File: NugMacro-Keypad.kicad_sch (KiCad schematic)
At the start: 16 parts

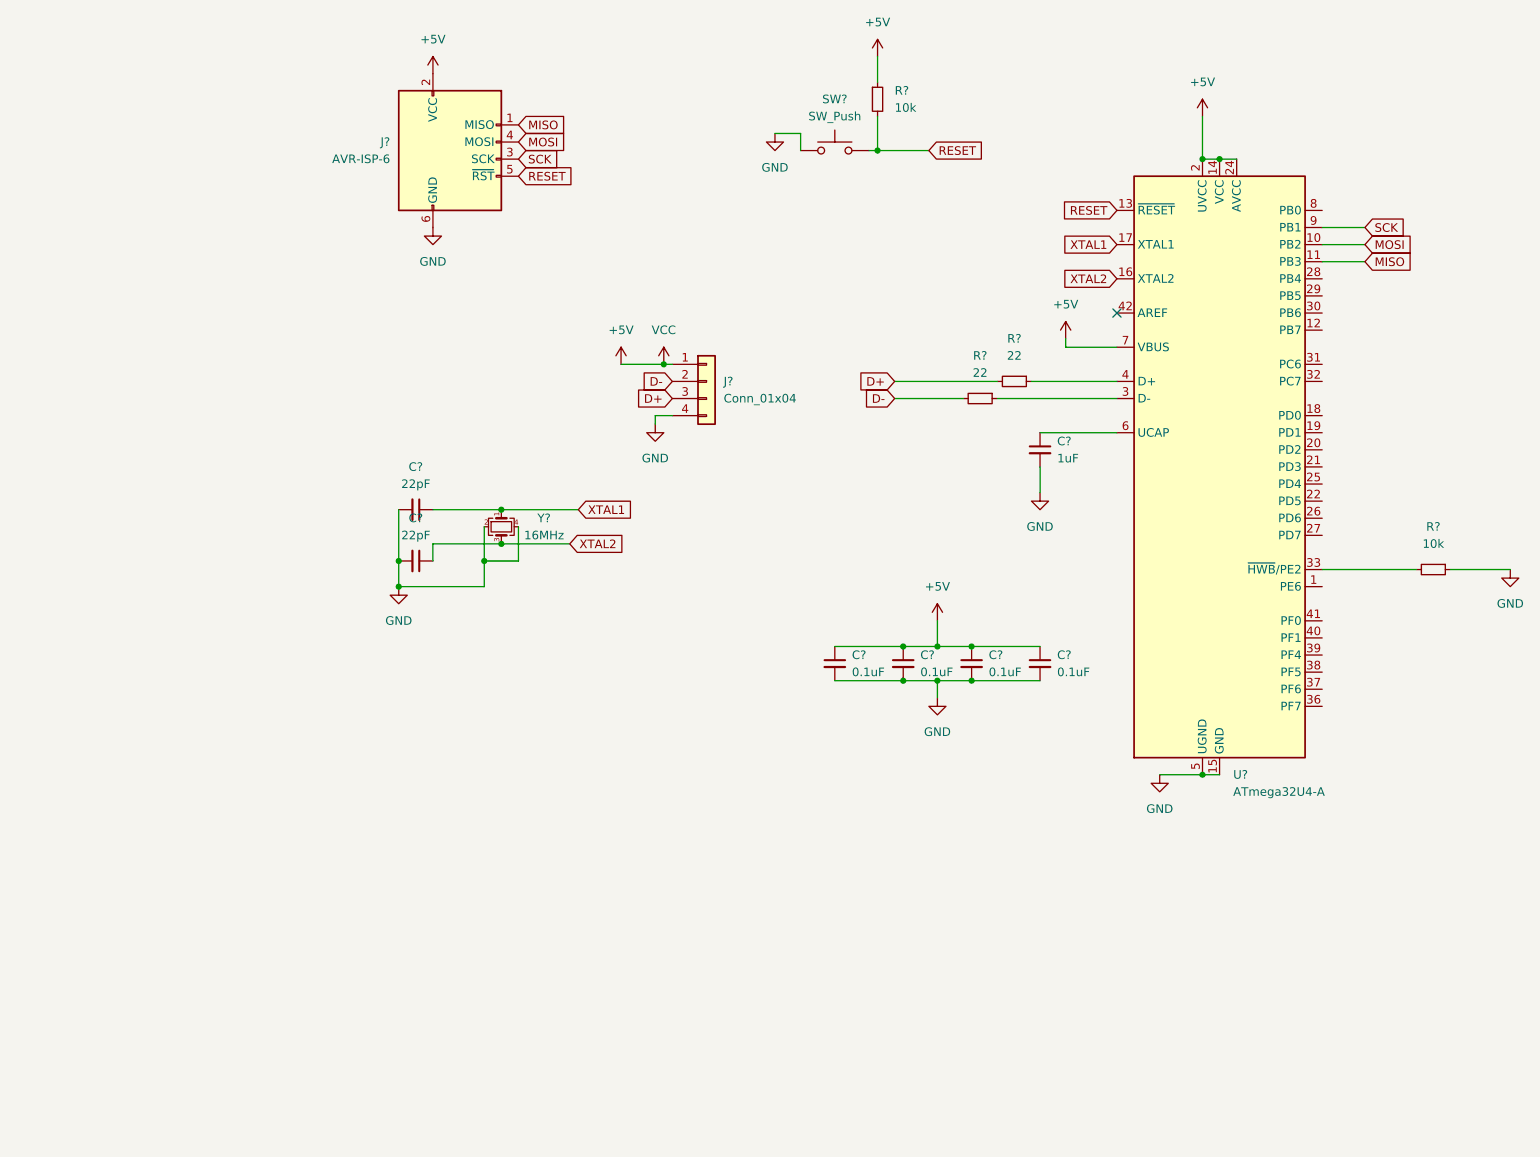
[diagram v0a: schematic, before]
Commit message: schema finished with footprints assigned
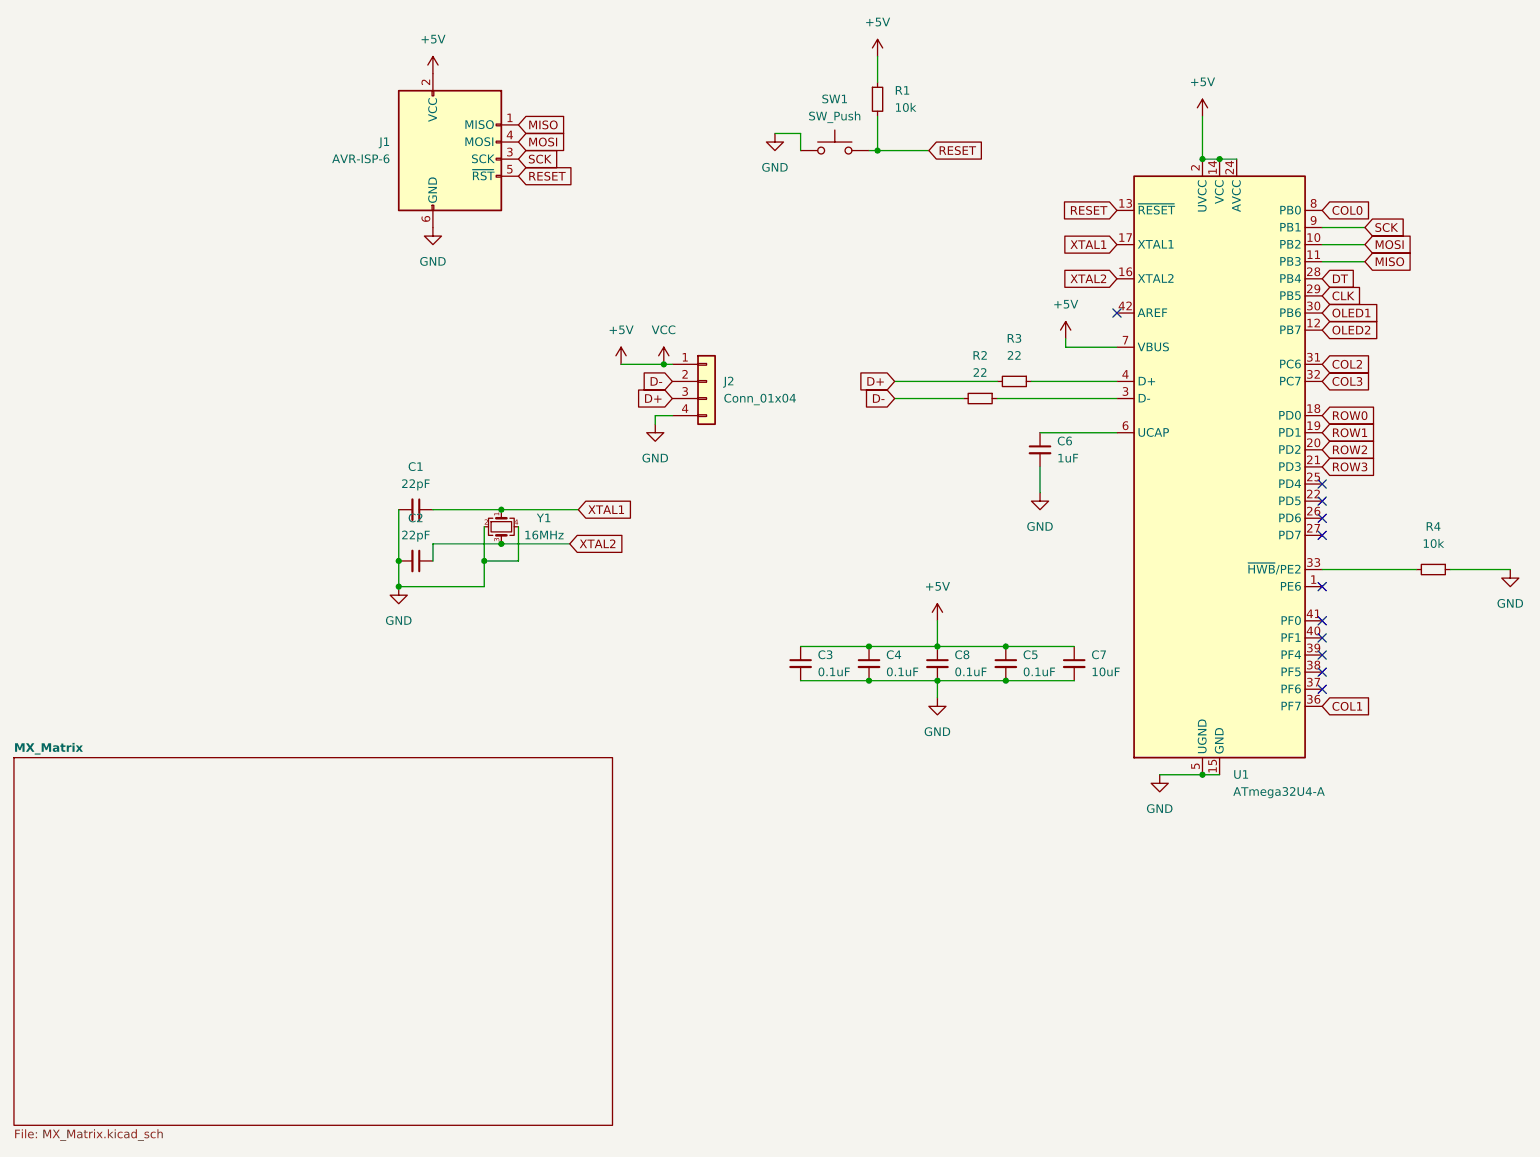
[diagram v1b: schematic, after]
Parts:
- added C8: 0.1uF, Capacitor_SMD:C_0805_2012Metric, symbol Device:C_Small
- C1, C2, C3, C4, C5, C6: renamed from C?; footprint (none) -> Capacitor_SMD:C_0805_2012Metric
- C7: renamed from C?; value 0.1uF -> 10uF; footprint (none) -> Capacitor_SMD:C_0805_2012Metric
- J1: renamed from J?; footprint (none) -> random-keyboard-parts:Reset_Pretty-Mask
- J2: renamed from J?; footprint (none) -> random-keyboard-parts:JST-SR-4
- R1, R2, R3, R4: renamed from R?; footprint (none) -> Resistor_SMD:R_0805_2012Metric
- SW1: renamed from SW?; footprint (none) -> random-keyboard-parts:SKQG-1155865
- Y1: renamed from Y?; footprint (none) -> Crystal:Crystal_SMD_3225-4Pin_3.2x2.5mm
- gave numbers to parts that had none: 1
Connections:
- net +5V: now also C8.1
- net GND: now also C8.2
- net OLED2: now reaches U1.12 (PB7)
- net ROW0: now reaches U1.18 (PD0)
- net ROW1: now reaches U1.19 (PD1)
- net ROW2: now reaches U1.20 (PD2)
- net ROW3: now reaches U1.21 (PD3)
- net DT: now reaches U1.28 (PB4)
- net CLK: now reaches U1.29 (PB5)
- net OLED1: now reaches U1.30 (PB6)
- net COL2: now reaches U1.31 (PC6)
- net COL3: now reaches U1.32 (PC7)
- net COL1: now reaches U1.36 (PF7)
- net COL0: now reaches U1.8 (PB0)
- no-connect marks 1 -> 11
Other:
- added sheet MX_Matrix (MX_Matrix.kicad_sch)
- moved on the sheet: C3, C4, C5, C7

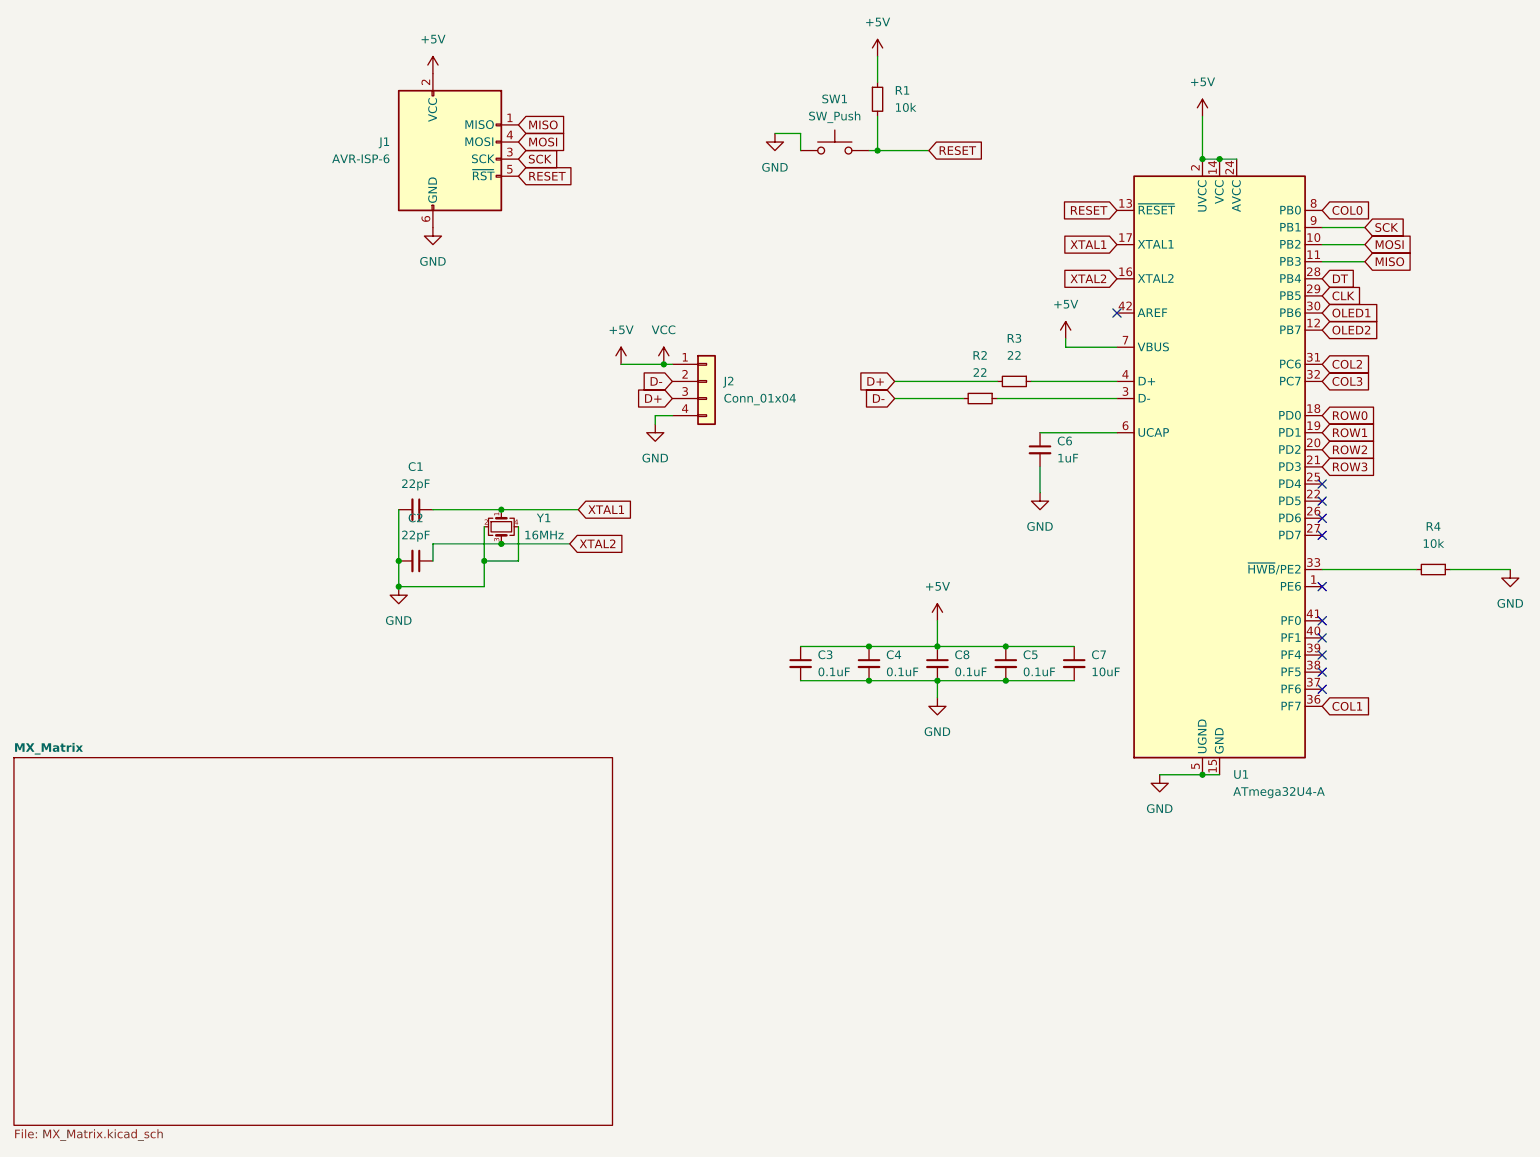
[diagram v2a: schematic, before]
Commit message: lil schema and pcb changes
flipped/ changed around smd components so it may be easier to route, got rid of reset pins for simplicity sake with small board
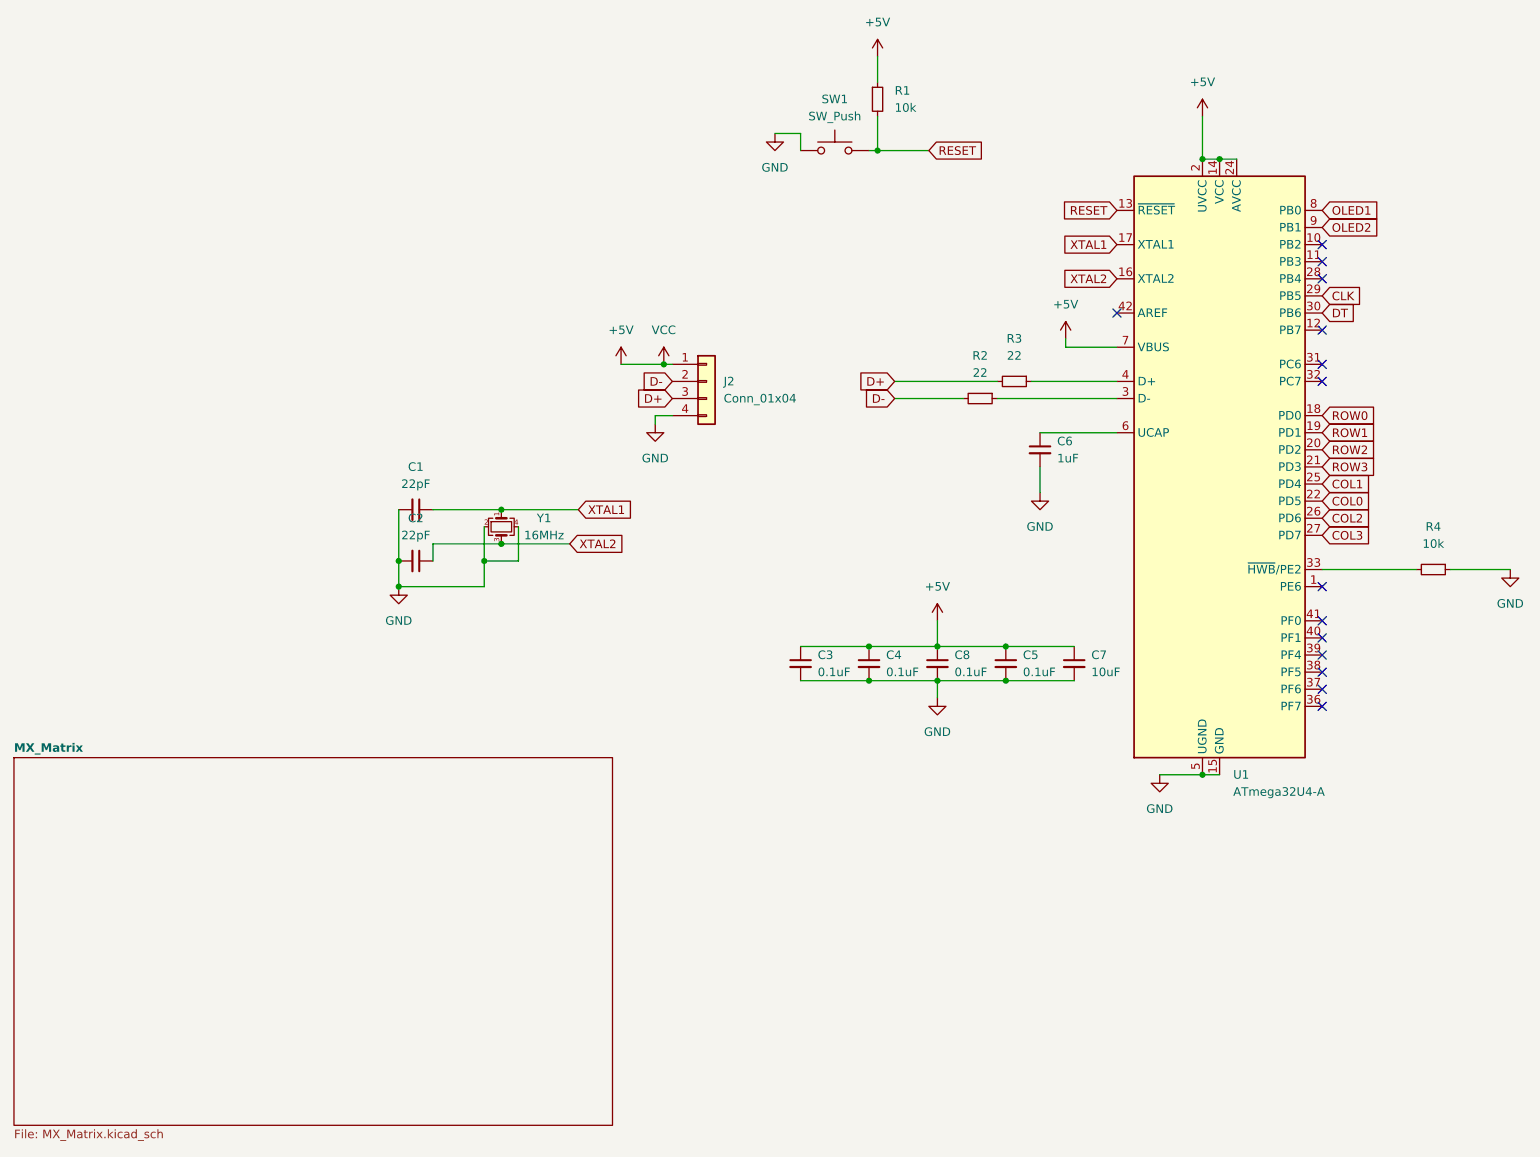
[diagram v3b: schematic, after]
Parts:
- removed J1: AVR-ISP-6, random-keyboard-parts:Reset_Pretty-Mask, symbol Connector:AVR-ISP-6
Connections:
- net SCK is gone; now on net OLED2: U1.9 (PB1)
- net COL0: now also U1.22 (PD5); no longer U1.8 (PB0)
- net COL1: now also U1.25 (PD4); no longer U1.36 (PF7)
- net COL2: now also U1.26 (PD6); no longer U1.31 (PC6)
- net COL3: now also U1.27 (PD7); no longer U1.32 (PC7)
- net DT: now also U1.30 (PB6); no longer U1.28 (PB4)
- net OLED1: now also U1.8 (PB0); no longer U1.30 (PB6)
- net OLED2: no longer U1.12 (PB7)
- net MISO: no longer names the net of U1.11 (PB3)
- net MOSI: no longer names the net of U1.10 (PB2)
- no-connect marks 11 -> 14

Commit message: First prototype pcb done
finally
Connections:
- net COL0: now also U1.37 (PF6); no longer U1.22 (PD5)
- net COL1: now also U1.36 (PF7); no longer U1.25 (PD4)
- net ROW0: now also U1.38 (PF5); no longer U1.18 (PD0)
- net ROW1: now also U1.39 (PF4); no longer U1.19 (PD1)
- net ROW2: now also U1.40 (PF1); no longer U1.20 (PD2)
- net ROW3: now also U1.41 (PF0); no longer U1.21 (PD3)
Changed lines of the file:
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@@
   (no_connect (at 195.58 71.12))
   (no_connect (at 226.06 73.66))
-  (no_connect (at 226.06 124.46))
+  (no_connect (at 226.06 88.9))
+  (no_connect (at 226.06 86.36))
+  (no_connect (at 226.06 96.52))
   (no_connect (at 226.06 81.28))
-  (no_connect (at 226.06 119.38))
   (no_connect (at 226.06 111.76))
-  (no_connect (at 226.06 129.54))
   (no_connect (at 226.06 60.96))
+  (no_connect (at 226.06 93.98))
   (no_connect (at 226.06 63.5))
-  (no_connect (at 226.06 121.92))
-  (no_connect (at 226.06 127))
-  (no_connect (at 226.06 116.84))
+  (no_connect (at 226.06 91.44))
+  (no_connect (at 226.06 99.06))
   (no_connect (at 226.06 66.04))
   (no_connect (at 226.06 78.74))
@@
     )
   )
-  (global_label "ROW3" (shape input) (at 226.06 93.98 0) (fields_autoplaced)
-    (effects (font (size 1.27 1.27)) (justify left))
-    (property "Intersheet References" "${INTERSHEET_REFS}" (id 0) (at 233.7345 93.9006 0)
+  (global_label "ROW3" (shape input) (at 226.06 116.84 0) (fields_autoplaced)
+    (effects (font (size 1.27 1.27)) (justify left))
+    (property "Intersheet References" "${INTERSHEET_REFS}" (id 0) (at 233.7345 116.7606 0)
       (effects (font (size 1.27 1.27)) (justify left) hide)
     )
@@
     )
   )
-  (global_label "ROW0" (shape input) (at 226.06 86.36 0) (fields_autoplaced)
-    (effects (font (size 1.27 1.27)) (justify left))
-    (property "Intersheet References" "${INTERSHEET_REFS}" (id 0) (at 233.7345 86.2806 0)
+  (global_label "ROW0" (shape input) (at 226.06 124.46 0) (fields_autoplaced)
+    (effects (font (size 1.27 1.27)) (justify left))
+    (property "Intersheet References" "${INTERSHEET_REFS}" (id 0) (at 233.7345 124.3806 0)
       (effects (font (size 1.27 1.27)) (justify left) hide)
     )
@@
     )
   )
-  (global_label "COL0" (shape input) (at 226.06 99.06 0) (fields_autoplaced)
-    (effects (font (size 1.27 1.27)) (justify left))
-    (property "Intersheet References" "${INTERSHEET_REFS}" (id 0) (at 233.3112 98.9806 0)
+  (global_label "COL0" (shape input) (at 226.06 127 0) (fields_autoplaced)
+    (effects (font (size 1.27 1.27)) (justify left))
+    (property "Intersheet References" "${INTERSHEET_REFS}" (id 0) (at 233.3112 126.9206 0)
       (effects (font (size 1.27 1.27)) (justify left) hide)
     )
@@
     )
   )
-  (global_label "ROW1" (shape input) (at 226.06 88.9 0) (fields_autoplaced)
-    (effects (font (size 1.27 1.27)) (justify left))
-    (property "Intersheet References" "${INTERSHEET_REFS}" (id 0) (at 233.7345 88.8206 0)
+  (global_label "ROW1" (shape input) (at 226.06 121.92 0) (fields_autoplaced)
+    (effects (font (size 1.27 1.27)) (justify left))
+    (property "Intersheet References" "${INTERSHEET_REFS}" (id 0) (at 233.7345 121.8406 0)
       (effects (font (size 1.27 1.27)) (justify left) hide)
     )
@@
     )
   )
-  (global_label "COL1" (shape input) (at 226.06 96.52 0) (fields_autoplaced)
-    (effects (font (size 1.27 1.27)) (justify left))
-    (property "Intersheet References" "${INTERSHEET_REFS}" (id 0) (at 233.3112 96.4406 0)
+  (global_label "COL1" (shape input) (at 226.06 129.54 0) (fields_autoplaced)
+    (effects (font (size 1.27 1.27)) (justify left))
+    (property "Intersheet References" "${INTERSHEET_REFS}" (id 0) (at 233.3112 129.4606 0)
       (effects (font (size 1.27 1.27)) (justify left) hide)
     )
@@
     )
   )
-  (global_label "ROW2" (shape input) (at 226.06 91.44 0) (fields_autoplaced)
-    (effects (font (size 1.27 1.27)) (justify left))
-    (property "Intersheet References" "${INTERSHEET_REFS}" (id 0) (at 233.7345 91.3606 0)
-      (effects (font (size 1.27 1.27)) (justify left) hide)
-    )
+  (global_label "ROW2" (shape input) (at 226.06 119.38 0) (fields_autoplaced)
+    (effects (font (size 1.27 1.27)) (justify left))
+    (property "Intersheet References" "${INTERSHEET_REFS}" (id 0) (at 233.7345 119.3006 0)
+      (effects (font (size 1.27 1.27)) (justify left) hide)
+    )

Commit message: its done
yay
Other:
- company: MIT Liscence -> MIT License
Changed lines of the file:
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@@
     (title "Nug Macro V3")
     (rev "V3")
-    (company "MIT Liscence")
+    (company "MIT License")
   )
   (junction (at 88.9 111.76) (diameter 0) (color 0 0 0 0)
